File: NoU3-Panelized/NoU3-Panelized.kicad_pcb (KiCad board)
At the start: 4 copper layers, 154 x 174 mm, 1062 parts, among them J1 JST SR/SZ, J10 JST SR/SZ, J11 Screw_Terminal_01x02, J12 Screw_Terminal_01x02, J13 JST SR/SZ, J14 RFANT3216120A5T, J15 Barrel_Jack, J16 VIN, J17 JST SR/SZ, J18 GND, J19 JST SR/SZ, J2 Screw_Terminal_01x02, J3 Screw_Terminal_01x02, J4 JST SR/SZ, J5 Screw_Terminal_01x02, J6 Screw_Terminal_01x02, J7 JST SR/SZ, J8 Screw_Terminal_01x02, J9 Screw_Terminal_01x02, Q1 AO3401A, SW1 reset, SW2 boot, U1 HR8833, U10 PCA9685BS, U11 Qwiic1, U15 SY8113BADC, U16 SY8113BADC, U17 USB_C_Receptacle, U18 ServoPorts_2x3, U19 ServoPorts_2x3, U2 ESP32-S3FN8, U26 LSM6DSDTR, U3 Crystal_ESP32, U4 HR8833, U5 HR8833, U6 HR8833, U7 ServoPorts_2x3, U8 5.8 ZSPT, U9 USBLC6-2P6

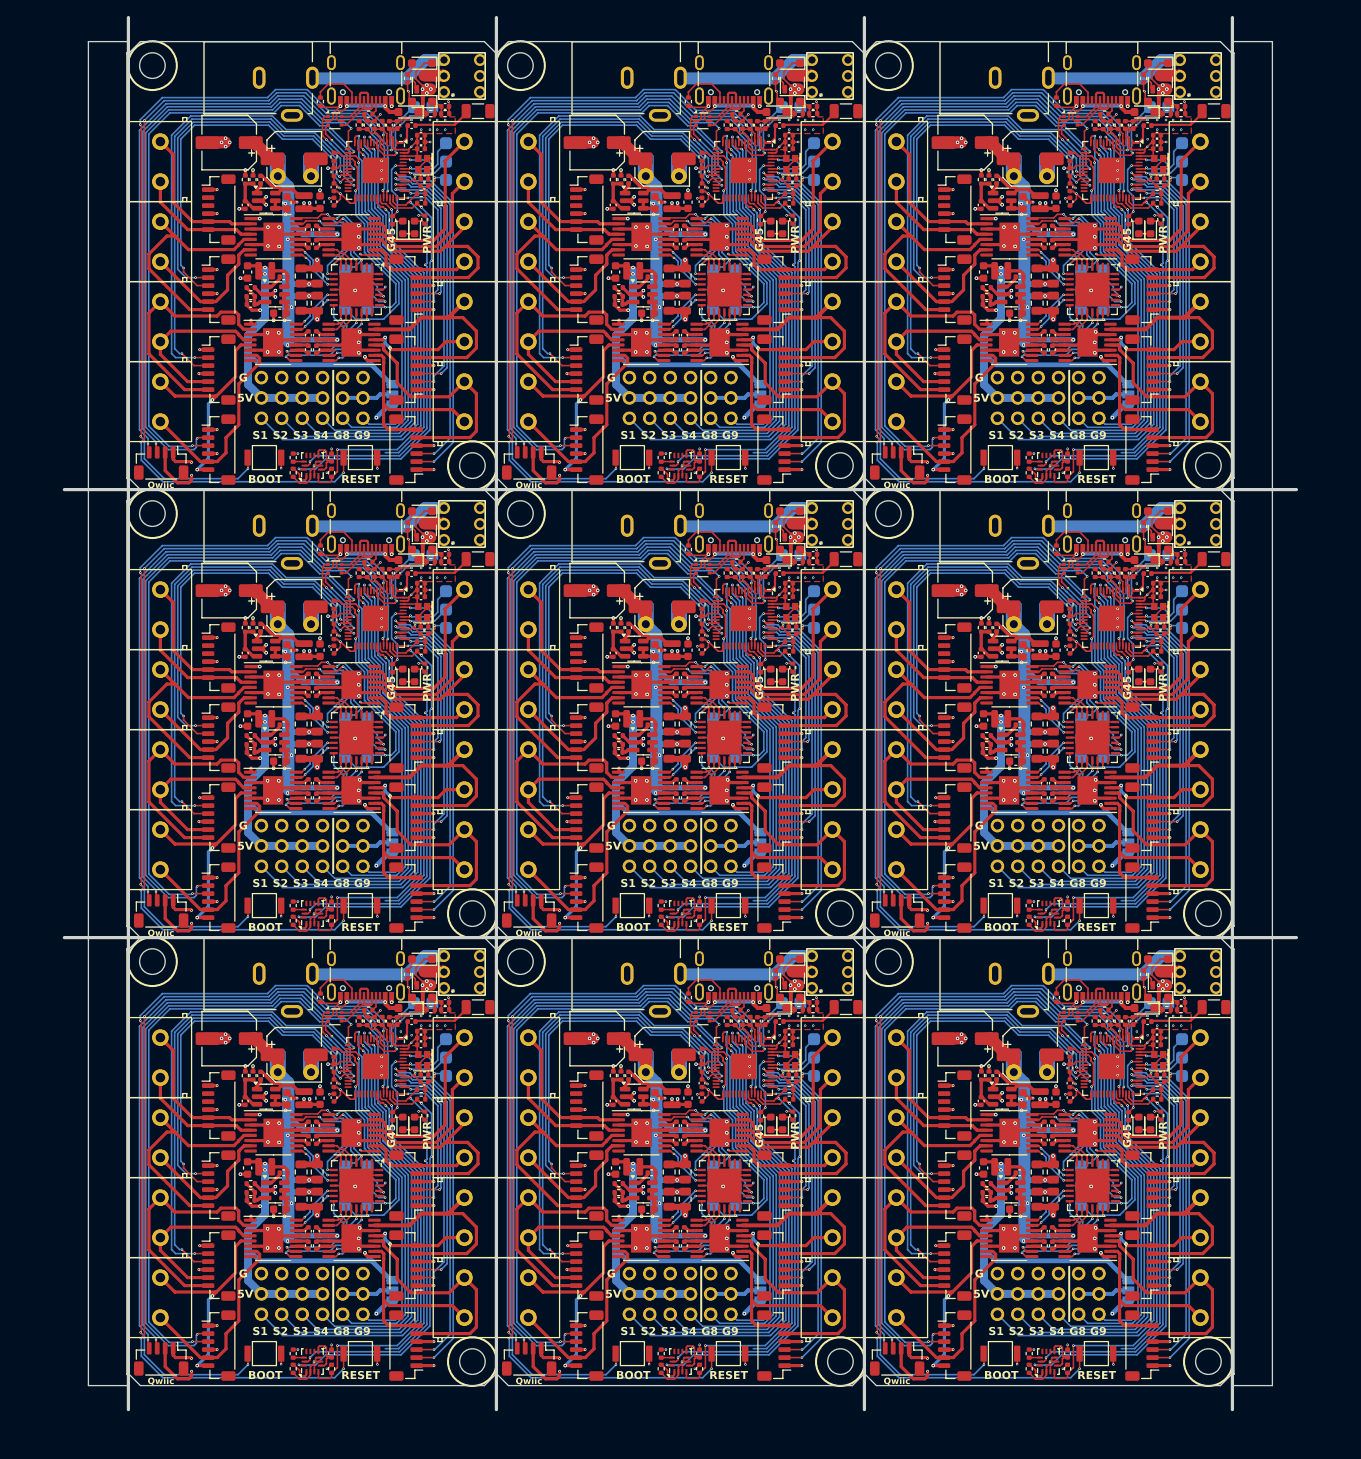
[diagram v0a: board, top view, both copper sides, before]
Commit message: Panel updates for next production run, removed version sns
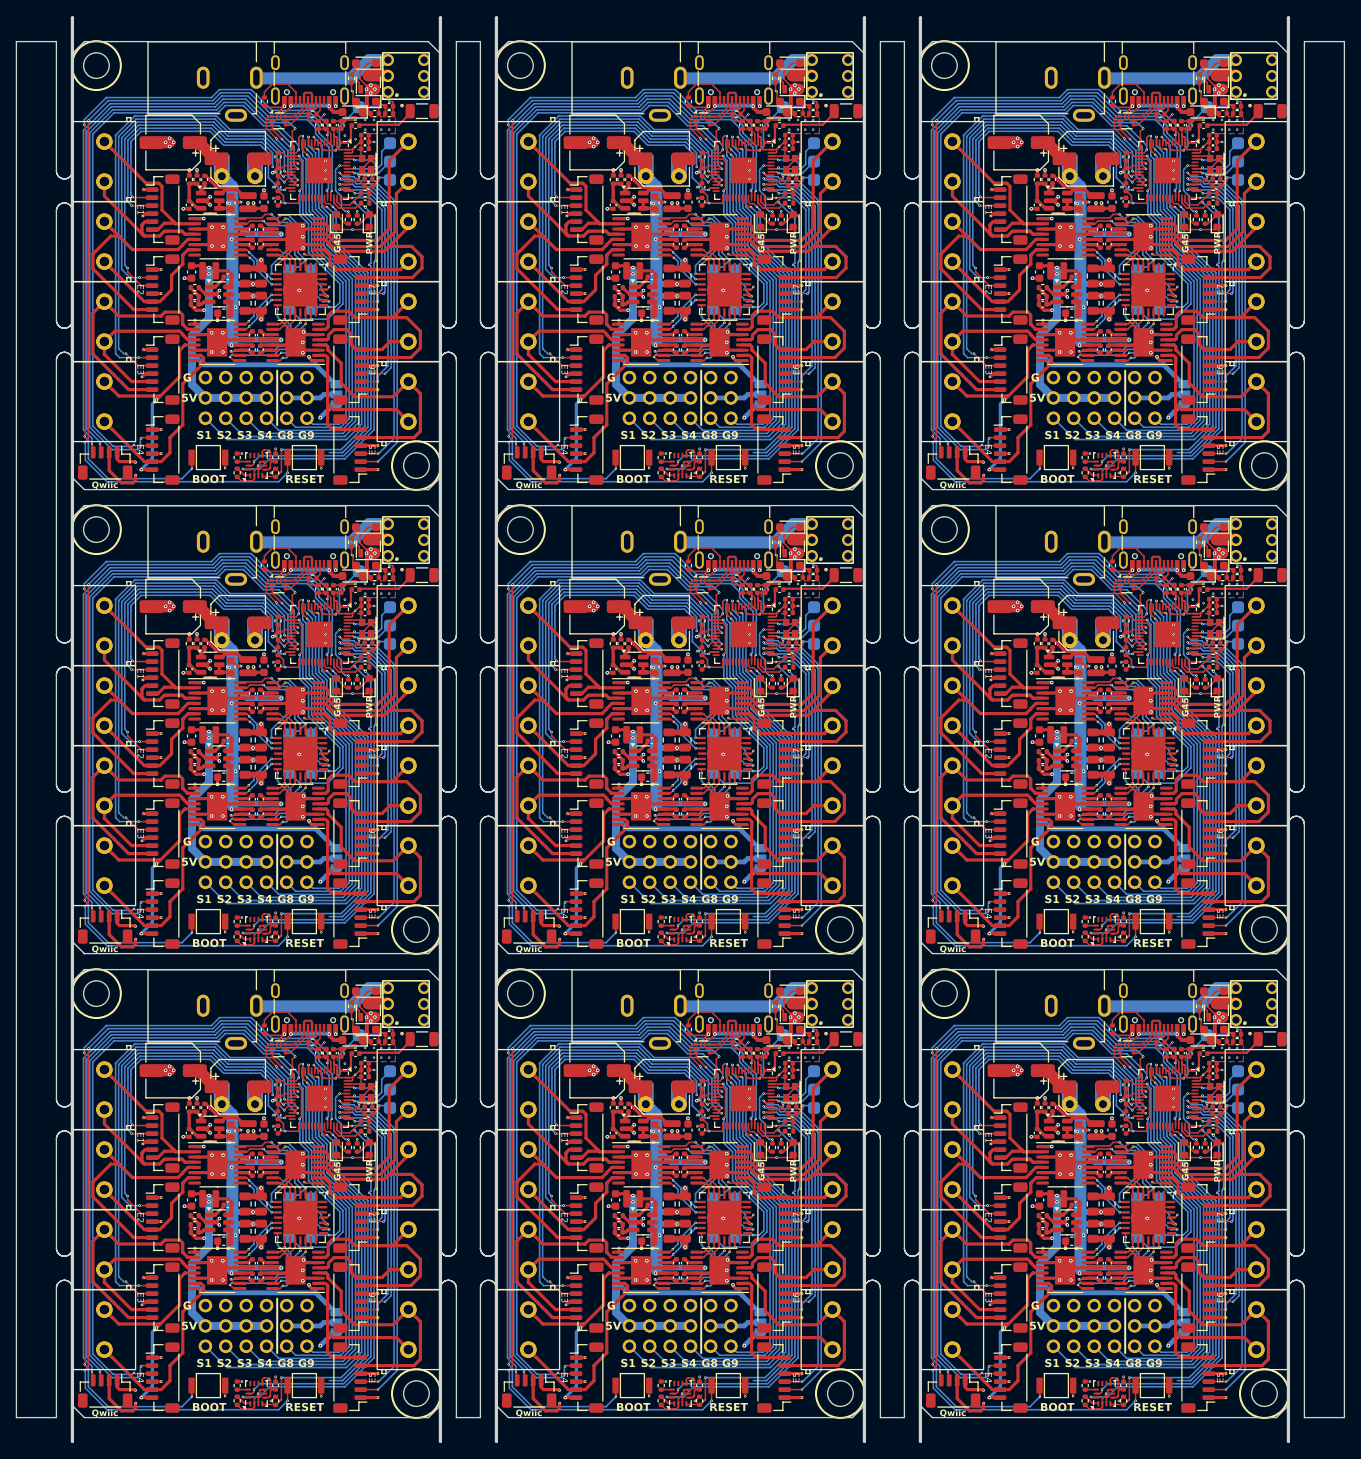
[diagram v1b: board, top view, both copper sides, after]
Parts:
- removed ? (x18): , 
- removed the C1 at (156.3, 86.4)
- removed the C1 at (202.3, 142.4)
- removed the C1 at (202.3, 30.4)
- removed the C1 at (156.3, 142.4)
- removed the C1 at (110.3, 142.4)
- removed the C1 at (202.3, 86.4)
- removed the C1 at (110.3, 30.4)
- removed the C1 at (110.3, 86.4)
- removed the C10 at (194.0, 56.7)
- removed the C10 at (194.0, 168.7)
- removed the C10 at (102.0, 168.7)
- removed the C10 at (148.0, 112.7)
- removed the C10 at (194.0, 112.7)
- removed the C10 at (102.0, 112.7)
- removed the C10 at (102.0, 56.7)
- removed the C10 at (148.0, 168.7)
- removed the C11 at (193.1, 49.3)
- removed the C11 at (101.1, 105.3)
- removed the C11 at (101.1, 161.3)
- removed the C11 at (193.1, 161.3)
- removed the C11 at (147.1, 161.3)
- removed the C11 at (101.1, 49.3)
- removed the C11 at (147.1, 105.3)
- removed the C11 at (193.1, 105.3)
- removed the C12 at (149.0, 168.7)
- removed the C12 at (195.0, 56.7)
- removed the C12 at (103.0, 112.7)
- removed the C12 at (195.0, 112.7)
- removed the C12 at (149.0, 112.7)
- removed the C12 at (103.0, 56.7)
- removed the C12 at (195.0, 168.7)
- removed the C12 at (103.0, 168.7)
- removed the C13 at (103.0, 58.5)
- removed the C13 at (195.0, 170.5)
- removed the C13 at (103.0, 114.5)
- removed the C13 at (149.0, 170.5)
- removed the C13 at (195.0, 114.5)
- removed the C13 at (149.0, 114.5)
- removed the C13 at (103.0, 170.5)
- removed the C13 at (195.0, 58.5)
- removed the C14 at (206.9, 86.5)
- removed the C14 at (114.9, 86.5)
- removed the C14 at (114.9, 142.5)
- removed the C14 at (160.9, 86.5)
- removed the C14 at (206.9, 142.5)
- removed the C14 at (160.9, 142.5)
- removed the C14 at (114.9, 30.5)
- removed the C14 at (206.9, 30.5)
- removed the C15 at (165.1, 140.1)
- removed the C15 at (211.1, 84.1)
- removed the C15 at (165.1, 84.1)
- removed the C15 at (211.1, 28.1)
- removed the C15 at (119.1, 84.1)
- removed the C15 at (119.1, 140.1)
- removed the C15 at (119.1, 28.1)
- removed the C15 at (211.1, 140.1)
- removed the C16 at (92.1, 88.6)
- removed the C16 at (184.1, 88.6)
- removed the C16 at (138.1, 88.6)
- removed the C16 at (184.1, 32.6)
- removed the C16 at (184.1, 144.6)
- removed the C16 at (92.1, 144.6)
- removed the C16 at (92.1, 32.6)
- removed the C16 at (138.1, 144.6)
- removed the C2 at (147.1, 164.7)
- removed the C2 at (193.1, 164.7)
- removed the C2 at (101.1, 52.7)
- removed the C2 at (101.1, 108.7)
- removed the C2 at (193.1, 108.7)
- removed the C2 at (147.1, 108.7)
- removed the C2 at (193.1, 52.7)
- removed the C2 at (101.1, 164.7)
- removed the C20 at (146.2, 90.7)
- removed the C20 at (146.2, 146.7)
- removed the C20 at (192.2, 146.7)
- removed the C20 at (100.2, 146.7)
- removed the C20 at (100.2, 90.7)
- removed the C20 at (192.2, 90.7)
- removed the C20 at (100.2, 34.6)
- removed the C20 at (192.2, 34.6)
- removed the C21 at (113.1, 86.4)
- removed the C21 at (205.1, 30.4)
- removed the C21 at (205.1, 142.4)
- removed the C21 at (113.1, 142.4)
- removed the C21 at (205.1, 86.4)
- removed the C21 at (113.1, 30.4)
- removed the C21 at (159.1, 142.4)
- removed the C21 at (159.1, 86.4)
- removed the C22 at (145.3, 96.2)
- removed the C22 at (99.3, 152.2)
- removed the C22 at (191.3, 96.2)
- removed the C22 at (99.3, 40.1)
- removed the C22 at (99.3, 96.2)
- removed the C22 at (191.3, 40.1)
- removed the C22 at (145.3, 152.2)
- removed the C22 at (191.3, 152.2)
- removed the C23 at (190.4, 165.9)
- removed the C23 at (144.4, 165.9)
- removed the C23 at (98.4, 54.0)
- removed the C23 at (98.4, 110.0)
- removed the C23 at (98.4, 165.9)
- removed the C23 at (190.4, 54.0)
- removed the C23 at (190.4, 110.0)
- removed the C23 at (144.4, 110.0)
- removed the C24 at (158.1, 142.4)
- removed the C24 at (204.1, 86.4)
- removed the C24 at (158.1, 86.4)
- removed the C24 at (112.1, 30.4)
- removed the C24 at (204.1, 30.4)
- removed the C24 at (204.1, 142.4)
- removed the C24 at (112.1, 142.4)
- removed the C24 at (112.1, 86.4)
- removed the C25 at (197.2, 148.3)
- removed the C25 at (197.2, 92.3)
- removed the C25 at (105.2, 92.3)
- removed the C25 at (151.2, 92.3)
- removed the C25 at (105.2, 148.3)
- removed the C25 at (197.2, 36.3)
- removed the C25 at (151.2, 148.3)
- removed the C25 at (105.2, 36.3)
- removed the C26 at (105.2, 150.2)
- removed the C26 at (151.2, 94.2)
- removed the C26 at (151.2, 150.2)
- removed the C26 at (197.2, 38.2)
- removed the C26 at (105.2, 94.2)
- removed the C26 at (105.2, 38.2)
- removed the C26 at (197.2, 150.2)
- removed the C26 at (197.2, 94.2)
- removed the C27 at (105.2, 152.0)
- removed the C27 at (197.2, 40.0)
- removed the C27 at (197.2, 152.0)
- removed the C27 at (105.2, 96.0)
- removed the C27 at (151.2, 152.0)
- removed the C27 at (197.2, 96.0)
- removed the C27 at (151.2, 96.0)
- removed the C27 at (105.2, 40.0)
- removed the C28 at (188.0, 37.2)
- removed the C28 at (96.0, 149.2)
- removed the C28 at (96.0, 93.2)
- removed the C28 at (188.0, 93.2)
- removed the C28 at (142.0, 149.2)
- removed the C28 at (96.0, 37.2)
- removed the C28 at (188.0, 149.2)
- removed the C28 at (142.0, 93.2)
- removed the C29 at (144.9, 105.4)
- removed the C29 at (190.9, 105.4)
- removed the C29 at (98.9, 161.4)
- removed the C29 at (144.9, 161.4)
- removed the C29 at (190.9, 161.4)
- removed the C29 at (190.9, 49.4)
- removed the C29 at (98.9, 49.4)
- removed the C29 at (98.9, 105.4)
- removed the C3 at (103.0, 43.5)
- removed the C3 at (195.0, 155.5)
- removed the C3 at (103.0, 155.5)
- removed the C3 at (149.0, 155.5)
- removed the C3 at (195.0, 99.5)
- removed the C3 at (149.0, 99.5)
- removed the C3 at (103.0, 99.5)
- removed the C3 at (195.0, 43.5)
- removed the C30 at (208.5, 150.1)
- removed the C30 at (208.5, 94.0)
- removed the C30 at (116.5, 150.1)
- removed the C30 at (162.5, 150.1)
- removed the C30 at (208.5, 38.0)
- removed the C30 at (162.5, 94.0)
- removed the C30 at (116.5, 38.0)
- removed the C30 at (116.5, 94.0)
- removed the C31 at (162.1, 143.7)
- removed the C31 at (208.1, 143.7)
- removed the C31 at (116.1, 87.7)
- removed the C31 at (208.1, 31.7)
- removed the C31 at (116.1, 31.7)
- removed the C31 at (162.1, 87.7)
- removed the C31 at (208.1, 87.7)
- removed the C31 at (116.1, 143.7)
- removed the C32 at (186.1, 40.4)
- removed the C32 at (140.1, 96.4)
- removed the C32 at (94.1, 96.4)
- removed the C32 at (94.1, 40.4)
- removed the C32 at (140.1, 152.4)
- removed the C32 at (186.1, 96.4)
- removed the C32 at (94.1, 152.4)
- removed the C32 at (186.1, 152.4)
- removed the C33 at (186.8, 52.9)
- removed the C33 at (140.8, 108.8)
- removed the C33 at (140.8, 164.8)
- removed the C33 at (94.8, 108.8)
- removed the C33 at (94.8, 52.9)
- removed the C33 at (186.8, 108.8)
- removed the C33 at (94.8, 164.8)
- removed the C33 at (186.8, 164.8)
- removed the C34 at (162.1, 88.5)
- removed the C34 at (116.1, 88.5)
- removed the C34 at (116.1, 144.6)
- removed the C34 at (208.1, 32.5)
- removed the C34 at (116.1, 32.5)
- removed the C34 at (208.1, 144.6)
- removed the C34 at (208.1, 88.5)
- removed the C34 at (162.1, 144.6)
- removed the C35 at (103.5, 152.1)
- removed the C35 at (195.4, 152.1)
- removed the C35 at (103.5, 40.1)
- removed the C35 at (195.4, 96.1)
- removed the C35 at (149.4, 152.1)
- removed the C35 at (149.4, 96.1)
- removed the C35 at (195.4, 40.1)
- removed the C35 at (103.5, 96.1)
- removed the C36 at (140.4, 104.8)
- removed the C36 at (186.4, 160.8)
- removed the C36 at (94.4, 104.8)
- removed the C36 at (94.4, 48.8)
- removed the C36 at (186.4, 48.8)
- removed the C36 at (94.4, 160.8)
- removed the C36 at (186.4, 104.8)
- removed the C36 at (140.4, 160.8)
- removed the C37 at (116.1, 33.4)
- removed the C37 at (116.1, 89.4)
- removed the C37 at (208.1, 89.4)
- removed the C37 at (116.1, 145.4)
- removed the C37 at (162.1, 89.4)
- removed the C37 at (208.1, 145.4)
- removed the C37 at (162.1, 145.4)
- removed the C37 at (208.1, 33.4)
- removed the C38 at (162.5, 93.2)
- removed the C38 at (208.5, 93.2)
- removed the C38 at (116.5, 93.2)
- removed the C38 at (208.5, 149.2)
- removed the C38 at (116.5, 37.1)
- removed the C38 at (208.5, 37.1)
- removed the C38 at (116.5, 149.2)
- removed the C38 at (162.5, 149.2)
- removed the C4 at (195.0, 157.3)
- removed the C4 at (149.0, 157.3)
- removed the C4 at (103.0, 157.3)
- removed the C4 at (103.0, 101.3)
- removed the C4 at (195.0, 101.3)
- removed the C4 at (195.0, 45.3)
- removed the C4 at (103.0, 45.3)
- removed the C4 at (149.0, 101.3)
- removed the C40 at (150.9, 128.0)
- removed the C40 at (150.9, 184.0)
- removed the C40 at (104.9, 128.0)
- removed the C40 at (104.9, 184.0)
- removed the C40 at (196.9, 184.0)
- removed the C40 at (196.9, 72.0)
- removed the C40 at (104.9, 72.0)
- removed the C40 at (196.9, 128.0)
- removed the C5 at (149.1, 164.7)
- removed the C5 at (103.1, 164.7)
- removed the C5 at (103.1, 108.7)
- removed the C5 at (195.1, 108.7)
- removed the C5 at (149.1, 108.7)
- removed the C5 at (103.1, 52.7)
- removed the C5 at (195.1, 164.7)
- removed the C5 at (195.1, 52.7)
- removed the C6 at (148.0, 157.3)
- removed the C6 at (148.0, 101.3)
- removed the C6 at (102.0, 157.3)
- removed the C6 at (194.0, 157.3)
- removed the C6 at (102.0, 45.3)
- removed the C6 at (102.0, 101.3)
- removed the C6 at (194.0, 101.3)
- removed the C6 at (194.0, 45.3)
- removed the C7 at (194.0, 43.5)
- removed the C7 at (148.0, 155.5)
- removed the C7 at (194.0, 99.5)
- removed the C7 at (102.0, 99.5)
- removed the C7 at (194.0, 155.5)
- removed the C7 at (102.0, 43.5)
- removed the C7 at (148.0, 99.5)
- removed the C7 at (102.0, 155.5)
- removed the C8 at (195.1, 49.3)
- removed the C8 at (103.1, 105.3)
- removed the C8 at (195.1, 105.3)
- removed the C8 at (149.1, 105.3)
- removed the C8 at (103.1, 49.3)
- removed the C8 at (149.1, 161.3)
- removed the C8 at (195.1, 161.3)
- removed the C8 at (103.1, 161.3)
- removed the C9 at (148.0, 114.5)
- removed the C9 at (102.0, 114.5)
- removed the C9 at (194.0, 114.5)
- removed the C9 at (148.0, 170.5)
- removed the C9 at (194.0, 58.5)
- removed the C9 at (102.0, 58.5)
- removed the C9 at (194.0, 170.5)
- removed the C9 at (102.0, 170.5)
- removed the D1 at (208.2, 22.7)
- removed the D1 at (116.2, 22.7)
- removed the D1 at (208.2, 134.7)
- removed the D1 at (162.2, 134.7)
- removed the D1 at (162.2, 78.7)
- removed the D1 at (116.2, 78.7)
- removed the D1 at (116.2, 134.7)
- removed the D1 at (208.2, 78.7)
- removed the D2 at (206.5, 28.8)
- removed the D2 at (114.5, 84.8)
- removed the D2 at (160.5, 140.8)
- removed the D2 at (114.5, 28.8)
- removed the D2 at (160.5, 84.8)
- removed the D2 at (206.5, 84.8)
- removed the D2 at (114.5, 140.8)
- removed the D2 at (206.5, 140.8)
- removed the D3 at (208.2, 83.5)
- removed the D3 at (116.2, 27.5)
- removed the D3 at (208.2, 27.5)
- removed the D3 at (116.2, 83.5)
- removed the D3 at (162.2, 139.5)
- removed the D3 at (162.2, 83.5)
- removed the D3 at (116.2, 139.5)
- removed the D3 at (208.2, 139.5)
- removed the D5 at (115.3, 43.2)
- removed the D5 at (115.3, 99.2)
- removed the D5 at (115.3, 155.2)
- removed the D5 at (207.3, 155.2)
- removed the D5 at (207.3, 99.2)
- removed the D5 at (207.3, 43.2)
- removed the D5 at (161.3, 99.2)
- removed the D5 at (161.3, 155.2)
- removed the D5 at (161.3, 43.2)
- removed the D6 at (159.8, 155.2)
- removed the D6 at (113.8, 155.2)
- removed the D6 at (205.8, 155.2)
- removed the D6 at (113.8, 43.2)
- removed the D6 at (159.8, 99.2)
- removed the D6 at (205.8, 43.2)
- removed the D6 at (205.8, 99.2)
- removed the D6 at (113.8, 99.2)
- removed the D6 at (159.8, 43.2)
- removed the G*** at (91.6, 171.8)
- removed the G*** at (183.6, 171.8)
- removed the G*** at (87.1, 124.3)
- removed the G*** at (179.1, 124.3)
- removed the G*** at (183.6, 115.8)
- removed the G*** at (133.1, 180.3)
- removed the G*** at (137.6, 171.8)
- removed the G*** at (133.1, 124.3)
- removed the G*** at (183.6, 59.8)
- removed the G*** at (87.1, 180.3)
- removed the G*** at (137.6, 115.8)
- removed the G*** at (87.1, 68.3)
- removed the G*** at (179.1, 180.3)
- removed the G*** at (179.1, 68.3)
- removed the G*** at (91.6, 115.8)
- removed the G*** at (91.6, 59.8)
- removed the J1 at (160.2, 163.0)
- removed the J1 at (114.2, 51.0)
- removed the J1 at (114.2, 163.0)
- removed the J1 at (206.2, 107.0)
- removed the J1 at (206.2, 163.0)
- removed the J1 at (160.2, 107.0)
- removed the J1 at (206.2, 51.0)
- removed the J1 at (114.2, 107.0)
- removed the J10 at (206.2, 71.0)
- removed the J10 at (206.2, 127.0)
- removed the J10 at (206.2, 183.0)
- removed the J10 at (114.2, 71.0)
- removed the J10 at (114.2, 183.0)
- removed the J10 at (160.2, 183.0)
- removed the J10 at (114.2, 127.0)
- removed the J10 at (160.2, 127.0)
- removed the J11 at (167.5, 121.0)
- removed the J11 at (121.5, 65.0)
- removed the J11 at (121.5, 177.0)
- removed the J11 at (167.5, 177.0)
- removed the J11 at (121.5, 121.0)
- removed the J11 at (213.5, 177.0)
- removed the J11 at (213.5, 65.0)
- removed the J11 at (213.5, 121.0)
- removed the J12 at (167.5, 111.0)
- removed the J12 at (213.5, 55.0)
- removed the J12 at (213.5, 167.0)
- removed the J12 at (121.5, 167.0)
- removed the J12 at (167.5, 167.0)
- removed the J12 at (213.5, 111.0)
- removed the J12 at (121.5, 111.0)
- removed the J12 at (121.5, 55.0)
- removed the J13 at (90.8, 71.0)
- removed the J13 at (182.8, 71.0)
- removed the J13 at (136.8, 183.0)
- removed the J13 at (182.8, 183.0)
- removed the J13 at (136.8, 127.0)
- removed the J13 at (90.8, 183.0)
- removed the J13 at (90.8, 127.0)
- removed the J13 at (182.8, 127.0)
- removed the J14 at (215.2, 28.7)
- removed the J14 at (123.2, 140.7)
- removed the J14 at (215.2, 140.7)
- removed the J14 at (169.2, 84.7)
- removed the J14 at (169.2, 140.7)
- removed the J14 at (123.2, 84.7)
- removed the J14 at (123.2, 28.7)
- removed the J14 at (215.2, 84.7)
- removed the J15 at (89.0, 136.5)
- removed the J15 at (134.9, 80.5)
- removed the J15 at (89.0, 80.5)
- removed the J15 at (180.9, 80.5)
- removed the J15 at (180.9, 136.5)
- removed the J15 at (180.9, 24.5)
- removed the J15 at (89.0, 24.5)
- removed the J15 at (134.9, 136.5)
- removed the J16 at (190.2, 36.8)
- removed the J16 at (144.2, 92.8)
- removed the J16 at (98.2, 148.8)
- removed the J16 at (190.2, 92.8)
- removed the J16 at (190.2, 148.8)
- removed the J16 at (98.2, 36.8)
- removed the J16 at (98.2, 92.8)
- removed the J16 at (144.2, 148.8)
- removed the J17 at (206.2, 117.0)
- removed the J17 at (206.2, 61.0)
- removed the J17 at (114.2, 173.0)
- removed the J17 at (160.2, 117.0)
- removed the J17 at (160.2, 173.0)
- removed the J17 at (114.2, 117.0)
- removed the J17 at (114.2, 61.0)
- removed the J17 at (206.2, 173.0)
- removed the J18 at (148.3, 92.8)
- removed the J18 at (102.3, 148.8)
- removed the J18 at (194.3, 148.8)
- removed the J18 at (102.3, 36.8)
- removed the J18 at (102.3, 92.8)
- removed the J18 at (148.3, 148.8)
- removed the J18 at (194.3, 92.8)
- removed the J18 at (194.3, 36.8)
- removed the J19 at (182.8, 41.0)
- removed the J19 at (90.8, 97.0)
- removed the J19 at (136.8, 97.0)
- removed the J19 at (182.8, 153.0)
- removed the J19 at (136.8, 153.0)
- removed the J19 at (182.8, 97.0)
- removed the J19 at (90.8, 41.0)
- removed the J19 at (90.8, 153.0)
- removed the J2 at (121.5, 157.0)
- removed the J2 at (121.5, 45.0)
- removed the J2 at (167.5, 157.0)
- removed the J2 at (121.5, 101.0)
- removed the J2 at (213.5, 157.0)
- removed the J2 at (213.5, 101.0)
- removed the J2 at (167.5, 101.0)
- removed the J2 at (213.5, 45.0)
- removed the J3 at (213.5, 91.0)
- removed the J3 at (167.5, 91.0)
- removed the J3 at (213.5, 35.0)
- removed the J3 at (167.5, 147.0)
- removed the J3 at (121.5, 147.0)
- removed the J3 at (121.5, 35.0)
- removed the J3 at (121.5, 91.0)
- removed the J3 at (213.5, 147.0)
- removed the J4 at (182.8, 163.0)
- removed the J4 at (90.8, 163.0)
- removed the J4 at (90.8, 107.0)
- removed the J4 at (182.8, 51.0)
- removed the J4 at (90.8, 51.0)
- removed the J4 at (136.8, 107.0)
- removed the J4 at (182.8, 107.0)
- removed the J4 at (136.8, 163.0)
- removed the J5 at (83.5, 147.0)
- removed the J5 at (175.5, 147.0)
- removed the J5 at (129.5, 147.0)
- removed the J5 at (175.5, 91.0)
- removed the J5 at (83.5, 35.0)
- removed the J5 at (83.5, 91.0)
- removed the J5 at (175.5, 35.0)
- removed the J5 at (129.5, 91.0)
- removed the J6 at (175.5, 157.0)
- removed the J6 at (83.5, 157.0)
- removed the J6 at (129.5, 101.0)
- removed the J6 at (175.5, 101.0)
- removed the J6 at (175.5, 45.0)
- removed the J6 at (83.5, 45.0)
- removed the J6 at (83.5, 101.0)
- removed the J6 at (129.5, 157.0)
- removed the J7 at (136.8, 117.0)
- removed the J7 at (90.8, 173.0)
- removed the J7 at (182.8, 61.0)
- removed the J7 at (182.8, 173.0)
- removed the J7 at (90.8, 61.0)
- removed the J7 at (90.8, 117.0)
- removed the J7 at (136.8, 173.0)
- removed the J7 at (182.8, 117.0)
- removed the J8 at (175.5, 111.0)
- removed the J8 at (83.5, 111.0)
- removed the J8 at (175.5, 167.0)
- removed the J8 at (129.5, 167.0)
- removed the J8 at (129.5, 111.0)
- removed the J8 at (83.5, 55.0)
- removed the J8 at (175.5, 55.0)
- removed the J8 at (83.5, 167.0)
- removed the J9 at (175.5, 65.0)
- removed the J9 at (129.5, 121.0)
- removed the J9 at (83.5, 121.0)
- removed the J9 at (83.5, 65.0)
- removed the J9 at (175.5, 121.0)
- removed the J9 at (83.5, 177.0)
- removed the J9 at (129.5, 177.0)
- removed the J9 at (175.5, 177.0)
- removed the JP1 at (158.5, 176.1)
- removed the JP1 at (112.5, 120.1)
- removed the JP1 at (204.5, 64.1)
- removed the JP1 at (112.5, 64.1)
- removed the JP1 at (204.5, 176.1)
- removed the JP1 at (158.5, 120.1)
- removed the JP1 at (204.5, 120.1)
- removed the JP1 at (112.5, 176.1)
- removed the L1 at (101.5, 152.1)
- removed the L1 at (147.4, 152.1)
- removed the L1 at (101.5, 96.1)
- removed the L1 at (193.4, 152.1)
- removed the L1 at (193.4, 96.1)
- removed the L1 at (147.4, 96.1)
- removed the L1 at (193.4, 40.1)
- removed the L1 at (101.5, 40.1)
- removed the L2 at (96.6, 160.7)
- removed the L2 at (142.6, 160.7)
- removed the L2 at (188.6, 104.7)
- removed the L2 at (96.6, 48.6)
- removed the L2 at (188.6, 160.7)
- removed the L2 at (142.6, 104.7)
- removed the L2 at (188.6, 48.6)
- removed the L2 at (96.6, 104.7)
- removed the Q1 at (208.5, 137.1)
- removed the Q1 at (116.5, 137.1)
- removed the Q1 at (162.5, 81.1)
- removed the Q1 at (116.5, 81.1)
- removed the Q1 at (208.5, 81.1)
- removed the Q1 at (162.5, 137.1)
- removed the Q1 at (116.5, 25.1)
- removed the Q1 at (208.5, 25.1)
- removed the R10 at (114.4, 80.6)
- removed the R10 at (206.4, 136.6)
- removed the R10 at (114.4, 24.6)
- removed the R10 at (160.4, 80.6)
- removed the R10 at (206.4, 24.6)
- removed the R10 at (160.4, 136.6)
- removed the R10 at (114.4, 136.6)
- removed the R10 at (206.4, 80.6)
- removed the R11 at (186.1, 93.2)
- removed the R11 at (140.1, 93.2)
- removed the R11 at (186.1, 37.2)
- removed the R11 at (94.1, 37.2)
- removed the R11 at (140.1, 149.2)
- removed the R11 at (94.1, 149.2)
- removed the R11 at (186.1, 149.2)
- removed the R11 at (94.1, 93.2)
- removed the R12 at (141.1, 149.2)
- removed the R12 at (141.1, 93.2)
- removed the R12 at (187.1, 93.2)
- removed the R12 at (95.1, 149.2)
- removed the R12 at (187.1, 37.2)
- removed the R12 at (95.1, 37.2)
- removed the R12 at (187.1, 149.2)
- removed the R12 at (95.1, 93.2)
- removed the R13 at (94.8, 51.9)
- removed the R13 at (186.8, 107.9)
- removed the R13 at (140.8, 163.9)
- removed the R13 at (186.8, 51.9)
- removed the R13 at (140.8, 107.9)
- removed the R13 at (94.8, 107.9)
- removed the R13 at (94.8, 163.9)
- removed the R13 at (186.8, 163.9)
- removed the R14 at (94.8, 106.8)
- removed the R14 at (186.8, 162.8)
- removed the R14 at (140.8, 162.8)
- removed the R14 at (94.8, 50.8)
- removed the R14 at (186.8, 50.8)
- removed the R14 at (94.8, 162.8)
- removed the R14 at (186.8, 106.8)
- removed the R14 at (140.8, 106.8)
- removed the R15 at (155.5, 85.1)
- removed the R15 at (201.5, 29.1)
- removed the R15 at (201.5, 85.1)
- removed the R15 at (109.5, 141.1)
- removed the R15 at (109.5, 29.1)
- removed the R15 at (109.5, 85.1)
- removed the R15 at (201.5, 141.1)
- removed the R15 at (155.5, 141.1)
- removed the R16 at (103.5, 27.5)
- removed the R16 at (195.5, 27.5)
- removed the R16 at (103.5, 83.5)
- removed the R16 at (195.5, 139.5)
- removed the R16 at (149.5, 83.5)
- removed the R16 at (103.5, 139.5)
- removed the R16 at (195.5, 83.5)
- removed the R16 at (149.5, 139.5)
- removed the R17 at (162.6, 98.2)
- removed the R17 at (116.5, 154.2)
- removed the R17 at (208.6, 98.2)
- removed the R17 at (116.5, 98.2)
- removed the R17 at (208.6, 42.2)
- removed the R17 at (162.6, 154.2)
- removed the R17 at (116.5, 42.2)
- removed the R17 at (162.6, 42.2)
- removed the R17 at (208.6, 154.2)
- removed the R18 at (112.5, 98.3)
- removed the R18 at (112.5, 154.3)
- removed the R18 at (204.5, 154.3)
- removed the R18 at (204.5, 98.3)
- removed the R18 at (204.5, 42.3)
- removed the R18 at (158.5, 42.3)
- removed the R18 at (158.5, 154.3)
- removed the R18 at (112.5, 42.3)
- removed the R18 at (158.5, 98.3)
- removed the R19 at (192.1, 184.0)
- removed the R19 at (100.1, 72.0)
- removed the R19 at (192.1, 128.0)
- removed the R19 at (146.1, 184.0)
- removed the R19 at (100.1, 184.0)
- removed the R19 at (146.1, 128.0)
- removed the R19 at (192.1, 72.0)
- removed the R19 at (100.1, 128.0)
- removed the R20 at (208.1, 95.0)
- removed the R20 at (116.1, 151.0)
- removed the R20 at (208.1, 151.0)
- removed the R20 at (162.1, 151.0)
- removed the R20 at (162.1, 95.0)
- removed the R20 at (208.1, 39.0)
- removed the R20 at (116.1, 39.0)
- removed the R20 at (116.1, 95.0)
- removed the R21 at (162.1, 152.2)
- removed the R21 at (208.1, 40.2)
- removed the R21 at (116.1, 152.2)
- removed the R21 at (208.1, 96.2)
- removed the R21 at (208.1, 152.2)
- removed the R21 at (162.1, 96.2)
- removed the R21 at (116.1, 40.2)
- removed the R21 at (116.1, 96.2)
- removed the R22 at (192.1, 185.9)
- removed the R22 at (100.1, 129.9)
- removed the R22 at (100.1, 185.9)
- removed the R22 at (192.1, 73.9)
- removed the R22 at (192.1, 129.9)
- removed the R22 at (146.1, 129.9)
- removed the R22 at (100.1, 73.9)
- removed the R22 at (146.1, 185.9)
- removed the R23 at (197.2, 146.4)
- removed the R23 at (197.2, 90.4)
- removed the R23 at (105.2, 146.4)
- removed the R23 at (105.2, 90.4)
- removed the R23 at (151.2, 90.4)
- removed the R23 at (151.2, 146.4)
- removed the R23 at (105.2, 34.4)
- removed the R23 at (197.2, 34.4)
- removed the R24 at (196.9, 129.9)
- removed the R24 at (104.9, 129.9)
- removed the R24 at (104.9, 185.9)
- removed the R24 at (196.9, 185.9)
- removed the R24 at (150.9, 185.9)
- removed the R24 at (150.9, 129.9)
- removed the R24 at (196.9, 73.9)
- removed the R24 at (104.9, 73.9)
- removed the R26 at (163.3, 85.0)
- removed the R26 at (117.3, 85.0)
- removed the R26 at (209.3, 141.0)
- removed the R26 at (209.3, 85.0)
- removed the R26 at (117.3, 141.0)
- removed the R26 at (163.3, 141.0)
- removed the R26 at (117.3, 29.0)
- removed the R26 at (209.3, 29.0)
- removed the R27 at (165.1, 85.0)
- removed the R27 at (211.1, 141.0)
- removed the R27 at (119.1, 141.0)
- removed the R27 at (165.1, 141.0)
- removed the R27 at (211.1, 85.0)
- removed the R27 at (211.1, 29.0)
- removed the R27 at (119.1, 85.0)
- removed the R27 at (119.1, 29.0)
- removed R29 (x9): 3K, Resistor_SMD:R_0402_1005Metric
- removed R30 (x9): 5K, Resistor_SMD:R_0402_1005Metric
- removed the R5 at (157.2, 86.4)
- removed the R5 at (203.2, 86.4)
- removed the R5 at (203.2, 142.4)
- removed the R5 at (111.2, 30.4)
- removed the R5 at (111.2, 142.4)
- removed the R5 at (157.2, 142.4)
- removed the R5 at (111.2, 86.4)
- removed the R5 at (203.2, 30.4)
- removed the SW1 at (154.5, 184.0)
- removed the SW1 at (154.5, 128.0)
- removed the SW1 at (200.5, 72.0)
- removed the SW1 at (108.5, 128.0)
- removed the SW1 at (108.5, 184.0)
- removed the SW1 at (108.5, 72.0)
- removed the SW1 at (200.5, 128.0)
- removed the SW1 at (200.5, 184.0)
- removed the SW2 at (142.5, 184.0)
- removed the SW2 at (142.5, 128.0)
- removed the SW2 at (188.5, 184.0)
- removed the SW2 at (188.5, 128.0)
- removed the SW2 at (188.5, 72.0)
- removed the SW2 at (96.5, 128.0)
- removed the SW2 at (96.5, 72.0)
- removed the SW2 at (96.5, 184.0)
- removed the TP1 at (211.2, 147.0)
- removed the TP1 at (165.2, 147.0)
- removed the TP1 at (119.2, 147.0)
- removed the TP1 at (119.2, 91.0)
- removed the TP1 at (211.2, 35.0)
- removed the TP1 at (165.2, 91.0)
- removed the TP1 at (119.2, 35.0)
- removed the TP1 at (211.2, 91.0)
- removed the TP2 at (211.2, 88.7)
- removed the TP2 at (119.2, 32.7)
- removed the TP2 at (119.2, 88.7)
- removed the TP2 at (211.2, 32.7)
- removed the TP2 at (165.2, 144.7)
- removed the TP2 at (211.2, 144.7)
- removed the TP2 at (165.2, 88.7)
- removed the TP2 at (119.2, 144.7)
- removed the TP20 at (163.5, 28.2)
- removed the TP20 at (163.5, 84.2)
- removed the TP20 at (163.5, 140.2)
- removed the TP20 at (209.5, 84.2)
- removed the TP20 at (209.5, 28.2)
- removed the TP20 at (117.5, 84.2)
- removed the TP20 at (117.5, 28.2)
- removed the TP20 at (209.5, 140.2)
- removed the TP20 at (117.5, 140.2)
- removed TP21 (x9): Sver, AlfredoFootprints:PogoPad1
- removed the TP3 at (211.2, 37.3)
- removed the TP3 at (119.2, 93.3)
- removed the TP3 at (211.2, 93.3)
- removed the TP3 at (165.2, 149.3)
- removed the TP3 at (119.2, 37.3)
- removed the TP3 at (165.2, 93.3)
- removed the TP3 at (119.2, 149.3)
- removed the TP3 at (211.2, 149.3)
- removed the TP4 at (201.4, 109.4)
- removed the TP4 at (155.4, 109.4)
- removed the TP4 at (201.4, 53.4)
- removed the TP4 at (155.4, 165.4)
- removed the TP4 at (201.4, 165.4)
- removed the TP4 at (109.4, 53.4)
- removed the TP4 at (109.4, 165.4)
- removed the TP4 at (109.4, 109.4)
- removed the TP5 at (198.6, 160.6)
- removed the TP5 at (106.6, 104.6)
- removed the TP5 at (198.6, 48.6)
- removed the TP5 at (152.6, 104.6)
- removed the TP5 at (106.6, 160.6)
- removed the TP5 at (152.6, 160.6)
- removed the TP5 at (198.6, 104.6)
- removed the TP5 at (106.6, 48.6)
- removed the TP6 at (109.4, 163.1)
- removed the TP6 at (155.4, 163.1)
- removed the TP6 at (109.4, 107.1)
- removed the TP6 at (201.4, 51.1)
- removed the TP6 at (155.4, 107.1)
- removed the TP6 at (201.4, 107.1)
- removed the TP6 at (109.4, 51.1)
- removed the TP6 at (201.4, 163.1)
- removed the TP7 at (109.4, 104.6)
- removed the TP7 at (155.4, 160.6)
- removed the TP7 at (109.4, 160.6)
- removed the TP7 at (155.4, 104.6)
- removed the TP7 at (201.4, 160.6)
- removed the TP7 at (201.4, 48.6)
- removed the TP7 at (109.4, 48.6)
- removed the TP7 at (201.4, 104.6)
- removed the TP8 at (198.6, 53.4)
- removed the TP8 at (106.6, 165.4)
- removed the TP8 at (198.6, 165.4)
- removed the TP8 at (198.6, 109.4)
- removed the TP8 at (106.6, 53.4)
- removed the TP8 at (152.6, 109.4)
- removed the TP8 at (152.6, 165.4)
- removed the TP8 at (106.6, 109.4)
- removed the TP9 at (198.6, 163.1)
- removed the TP9 at (106.6, 107.1)
- removed the TP9 at (152.6, 163.1)
- removed the TP9 at (198.6, 51.1)
- removed the TP9 at (152.6, 107.1)
- removed the TP9 at (198.6, 107.1)
- removed the TP9 at (106.6, 163.1)
- removed the TP9 at (106.6, 51.1)
- removed the U1 at (107.4, 44.4)
- removed the U1 at (199.4, 100.4)
- removed the U1 at (107.4, 156.4)
- removed the U1 at (153.4, 100.4)
- removed the U1 at (199.4, 156.4)
- removed the U1 at (107.4, 100.4)
- removed the U1 at (153.4, 156.4)
- removed the U1 at (199.4, 44.4)
- removed the U10 at (108.0, 107.0)
- removed the U10 at (108.0, 51.0)
- removed the U10 at (154.0, 163.0)
- removed the U10 at (108.0, 163.0)
- removed the U10 at (200.0, 163.0)
- removed the U10 at (200.0, 51.0)
- removed the U10 at (200.0, 107.0)
- removed the U10 at (154.0, 107.0)
- removed the U11 at (83.6, 128.7)
- removed the U11 at (129.6, 128.7)
- removed the U11 at (83.6, 184.7)
- removed the U11 at (83.6, 72.7)
- removed the U11 at (129.6, 184.7)
- removed the U11 at (175.6, 128.7)
- removed the U11 at (175.6, 184.7)
- removed the U11 at (175.6, 72.7)
- removed the U15 at (142.7, 151.9)
- removed the U15 at (188.7, 39.9)
- removed the U15 at (96.7, 95.9)
- removed the U15 at (188.7, 151.9)
- removed the U15 at (96.7, 39.9)
- removed the U15 at (188.7, 95.9)
- removed the U15 at (96.7, 151.9)
- removed the U15 at (142.7, 95.9)
- removed the U16 at (97.9, 163.6)
- removed the U16 at (189.9, 163.6)
- removed the U16 at (189.9, 107.6)
- removed the U16 at (189.9, 51.6)
- removed the U16 at (97.9, 107.6)
- removed the U16 at (143.9, 163.6)
- removed the U16 at (97.9, 51.6)
- removed the U16 at (143.9, 107.6)
- removed the U17 at (201.2, 80.9)
- removed the U17 at (201.2, 24.9)
- removed the U17 at (201.2, 136.9)
- removed the U17 at (109.2, 24.9)
- removed the U17 at (155.2, 80.9)
- removed the U17 at (155.2, 136.9)
- removed the U17 at (109.2, 80.9)
- removed the U17 at (109.2, 136.9)
- removed the U18 at (98.7, 179.1)
- removed the U18 at (190.7, 123.1)
- removed the U18 at (190.7, 179.1)
- removed the U18 at (190.7, 67.1)
- removed the U18 at (144.7, 179.1)
- removed the U18 at (98.7, 123.1)
- removed the U18 at (144.7, 123.1)
- removed the U18 at (98.7, 67.1)
- removed the U19 at (149.8, 123.1)
- removed the U19 at (195.8, 67.1)
- removed the U19 at (103.8, 123.1)
- removed the U19 at (149.8, 179.1)
- removed the U19 at (195.8, 123.1)
- removed the U19 at (103.8, 179.1)
- removed the U19 at (195.8, 179.1)
- removed the U19 at (103.8, 67.1)
- removed the U2 at (202.4, 36.1)
- removed the U2 at (110.4, 36.1)
- removed the U2 at (202.4, 92.1)
- removed the U2 at (202.4, 148.1)
- removed the U2 at (156.4, 148.1)
- removed the U2 at (110.4, 92.1)
- removed the U2 at (110.4, 148.1)
- removed the U2 at (156.4, 92.1)
- removed the U26 at (102.5, 185.0)
- removed the U26 at (102.5, 73.0)
- removed the U26 at (148.5, 129.0)
- removed the U26 at (102.5, 129.0)
- removed the U26 at (194.5, 73.0)
- removed the U26 at (148.5, 185.0)
- removed the U26 at (194.5, 129.0)
- removed the U26 at (194.5, 185.0)
- removed the U3 at (116.3, 91.3)
- removed the U3 at (162.3, 91.3)
- removed the U3 at (116.3, 147.3)
- removed the U3 at (162.3, 147.3)
- removed the U3 at (208.3, 91.3)
- removed the U3 at (208.3, 147.3)
- removed the U3 at (116.3, 35.3)
- removed the U3 at (208.3, 35.3)
- removed the U4 at (143.6, 100.4)
- removed the U4 at (97.6, 100.4)
- removed the U4 at (97.6, 44.4)
- removed the U4 at (189.6, 156.4)
- removed the U4 at (143.6, 156.4)
- removed the U4 at (189.6, 44.4)
- removed the U4 at (97.6, 156.4)
- removed the U4 at (189.6, 100.4)
- removed the U5 at (189.6, 113.6)
- removed the U5 at (143.6, 169.6)
- removed the U5 at (97.6, 57.6)
- removed the U5 at (189.6, 57.6)
- removed the U5 at (97.6, 169.6)
- removed the U5 at (97.6, 113.6)
- removed the U5 at (143.6, 113.6)
- removed the U5 at (189.6, 169.6)
- removed the U6 at (199.4, 57.6)
- removed the U6 at (199.4, 113.6)
- removed the U6 at (153.4, 169.6)
- removed the U6 at (107.4, 57.6)
- removed the U6 at (199.4, 169.6)
- removed the U6 at (107.4, 169.6)
- removed the U6 at (153.4, 113.6)
- removed the U6 at (107.4, 113.6)
- removed the U7 at (200.8, 67.1)
- removed the U7 at (200.8, 123.1)
- removed the U7 at (108.8, 67.1)
- removed the U7 at (108.8, 179.1)
- removed the U7 at (200.8, 179.1)
- removed the U7 at (154.8, 123.1)
- removed the U7 at (108.8, 123.1)
- removed the U7 at (154.8, 179.1)
- removed the U8 at (121.2, 24.3)
- removed the U8 at (213.2, 24.3)
- removed the U8 at (213.2, 80.3)
- removed the U8 at (167.2, 136.3)
- removed the U8 at (167.2, 80.3)
- removed the U8 at (213.2, 136.3)
- removed the U8 at (121.2, 80.3)
- removed the U8 at (121.2, 136.3)
- removed the U9 at (197.3, 141.9)
- removed the U9 at (105.3, 141.9)
- removed the U9 at (151.3, 141.9)
- removed the U9 at (197.3, 85.9)
- removed the U9 at (105.3, 29.9)
- removed the U9 at (105.3, 85.9)
- removed the U9 at (197.3, 29.9)
- removed the U9 at (151.3, 85.9)
- added C1: 100nF, Capacitor_SMD:C_0402_1005Metric, F.Cu at (103.3, 146.4)
- added C1: 100nF, Capacitor_SMD:C_0402_1005Metric, F.Cu at (156.3, 146.4)
- added C1: 100nF, Capacitor_SMD:C_0402_1005Metric, F.Cu at (156.3, 88.4)
- added C1: 100nF, Capacitor_SMD:C_0402_1005Metric, F.Cu at (103.3, 30.4)
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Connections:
- J19 pad 5: Board_1-MD2_A1 -> Board_1-MD2_A2
- J19 pad 6: Board_1-MD2_A2 -> Board_1-MD2_A1
- U2 pad 19: Board_1-unconnected-(U2-GPIO14-Pad19) -> Board_1-E7A
- U2 pad 27: Board_1-unconnected-(U2-GPIO21-Pad27) -> Board_1-E7B
- U2 pad 6: Board_1-SNS_VER -> Board_1-unconnected-(U2-GPIO1-Pad6)
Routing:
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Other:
- board size 154 x 174 mm -> 166 x 178 mm
- board text added: "Alfredo NoU V3.6"
- board text added: "E1"
- board text added: "E2"
- board text added: "E3"
- board text added: "E4"
- board text added: "E5"
- board text added: "E6"
- board text added: "E7"
- board text added: "V"
- board text added: "X"
- board text removed: "Alfredo NoU V3.5"
- board text removed: "SVER"
